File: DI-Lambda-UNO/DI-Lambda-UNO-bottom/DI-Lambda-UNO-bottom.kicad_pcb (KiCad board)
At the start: 2 copper layers, 38.2 x 128.2 mm, 53 parts, among them J1 CONN_02X04, J10 CONN_02X04, J11 CONN_02X04, J13 CONN_02X04, J15 CONN_01X06, J16 CONN_01X06, J17 CONN_02X03, J18 USB_OTG, J2 Conn_01X01, J3 CONN_02X04, J4 Conn_01X01, J5 CONN_02X04, J6 CONN_02X04, J7 CONN_02X04, J8 CONN_02X04, J9 CONN_02X04, Q1 AO3400, SW1 RESET, U2 USBLC6-2SC6, U3 ATMEGA32U4-MU, U4 3.3v LDO, U5 AP3032, Y1 8Mhz

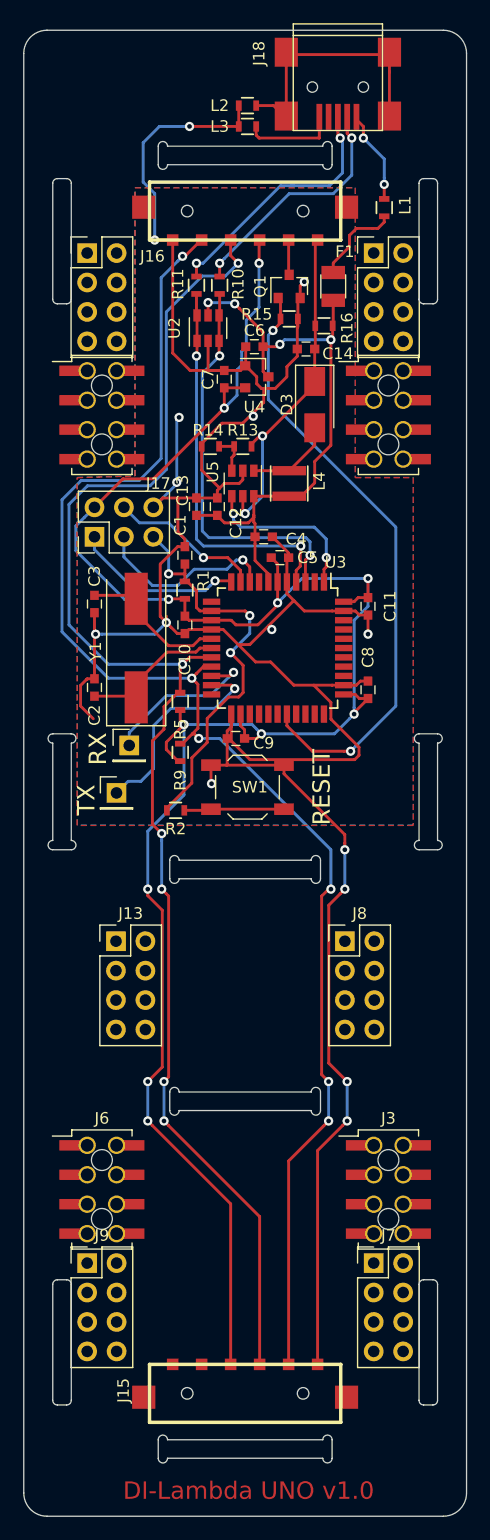
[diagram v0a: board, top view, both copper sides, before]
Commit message: Update connectors on the bottom plate
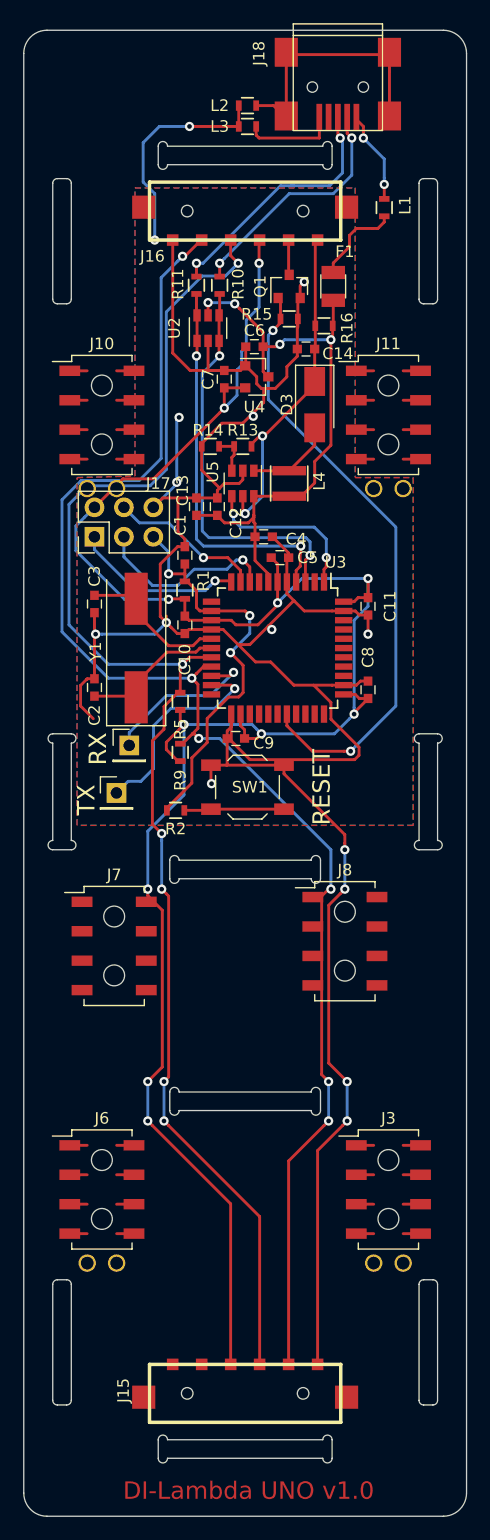
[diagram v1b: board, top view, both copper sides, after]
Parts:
- removed J1, J13, J5, J9: CONN_02X04, Pin_Headers:Pin_Header_Straight_2x04_Pitch2.54mm
- J10, J11, J3, J6: value CONN_02X04 -> CONN_02X05; footprint Female_socket_pitch254_smt_through-board:Pin_Header_Straight_2x04_Pitch2.54mm_SMD -> Female_socket_pitch254_smt_through-board:Pin_Header_Straight_2x04_Pitch2.54mm_SMD_2THT
- J7, J8: footprint Pin_Headers:Pin_Header_Straight_2x04_Pitch2.54mm -> Female_socket_pitch254_smt_through-board:Pin_Header_Straight_2x04_Pitch2.54mm_SMD
- moved J7 35.4 mm to (139.1, 115.0)

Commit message: Move spring connectors 0.3mm back on the bottom plate
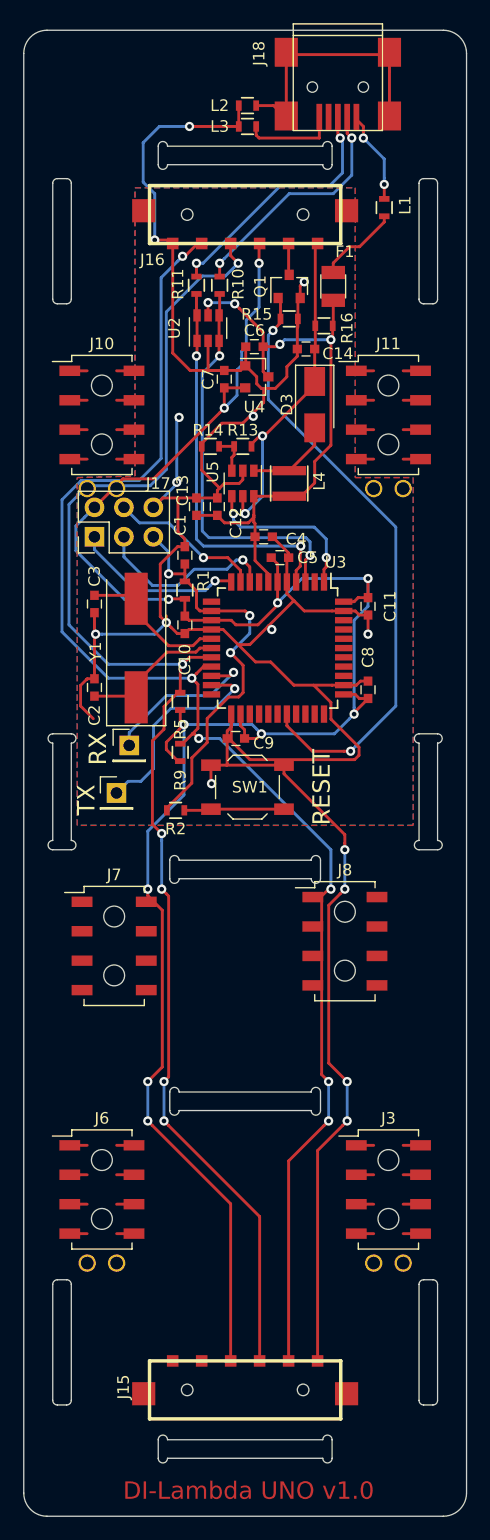
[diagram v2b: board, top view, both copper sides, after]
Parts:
- moved J16 0.30 mm to (150.4, 51.9)
- moved J15 0.30 mm to (150.4, 153.3)
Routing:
- net Net-(F1-Pad2): track 7.76 -> 7.18 mm
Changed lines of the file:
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@@
     (thickness 1.6)
     (drawings 106)
-    (tracks 628)
+    (tracks 625)
     (zones 0)
     (modules 49)
@@
   )
   (module Spring-contact-connector-2:Spring-contact-connector-2.5x6 (layer F.Cu)
-    (at 150.355 51.57 180)
+    (at 150.355 51.87 180)
     (fp_text reference J16 (at 8 -3.9) (layer F.SilkS)
       (effects (font (size 1 1) (thickness 0.15)))
@@
   )
   (module Spring-contact-connector-2:Spring-contact-connector-2.5x6 (layer F.Cu)
-    (at 150.355 153.57)
+    (at 150.355 153.27)
     (fp_text reference J15 (at -10.5 -0.25 90) (layer F.SilkS)
       (effects (font (size 1 1) (thickness 0.15)))
@@
   (segment (start 148.155 97.07) (end 157.755 106.67) (width 0.25) (layer B.Cu) (net 64))
   (segment (start 157.755 106.67) (end 157.755 110.07) (width 0.25) (layer B.Cu) (net 64))
+  (segment (start 157.955 56.87) (end 157.955 56.05) (width 0.25) (layer F.Cu) (net 68))
+  (segment (start 162.355 52.52) (end 162.355 52.02) (width 0.25) (layer F.Cu) (net 68))
+  (segment (start 157.955 56.05) (end 159.355 54.65) (width 0.25) (layer F.Cu) (net 68))
+  (segment (start 159.355 54.65) (end 160.225 54.65) (width 0.25) (layer F.Cu) (net 68))
+  (segment (start 160.225 54.65) (end 162.355 52.52) (width 0.25) (layer F.Cu) (net 68))
   (segment (start 142.355 104.47) (end 143.155 105.27) (width 0.25) (layer F.Cu) (net 72))
   (via (at 143.155 105.27) (size 0.8) (drill 0.4) (layers F.Cu B.Cu) (net 72))
@@
   (segment (start 149.055282 83.47) (end 149.155282 83.57) (width 0.25) (layer F.Cu) (net 67))
   (via (at 147.755 83.47) (size 0.8) (drill 0.4) (layers F.Cu B.Cu) (net 67))
-  (segment (start 159.955 53.07) (end 161.355 53.07) (width 0.25) (layer F.Cu) (net 68))
-  (segment (start 162.355 52.02) (end 162.355 52.52) (width 0.25) (layer F.Cu) (net 68))
-  (segment (start 162.355 52.52) (end 161.805 53.07) (width 0.25) (layer F.Cu) (net 68))
-  (segment (start 161.805 53.07) (end 161.355 53.07) (width 0.25) (layer F.Cu) (net 68))
-  (segment (start 159.355 53.67) (end 159.955 53.07) (width 0.25) (layer F.Cu) (net 68))
-  (segment (start 159.355 54.65) (end 159.355 53.67) (width 0.25) (layer F.Cu) (net 68))
-  (segment (start 157.955 56.87) (end 157.955 56.05) (width 0.25) (layer F.Cu) (net 68))
-  (segment (start 157.955 56.05) (end 159.355 54.65) (width 0.25) (layer F.Cu) (net 68))
   (segment (start 162.355 48.704315) (end 162.355 49.27) (width 0.25) (layer B.Cu) (net 69))
   (segment (start 162.355 47.073794) (end 162.355 48.704315) (width 0.25) (layer B.Cu) (net 69))

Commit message: Fix up the routing after connector update on the bottom plate
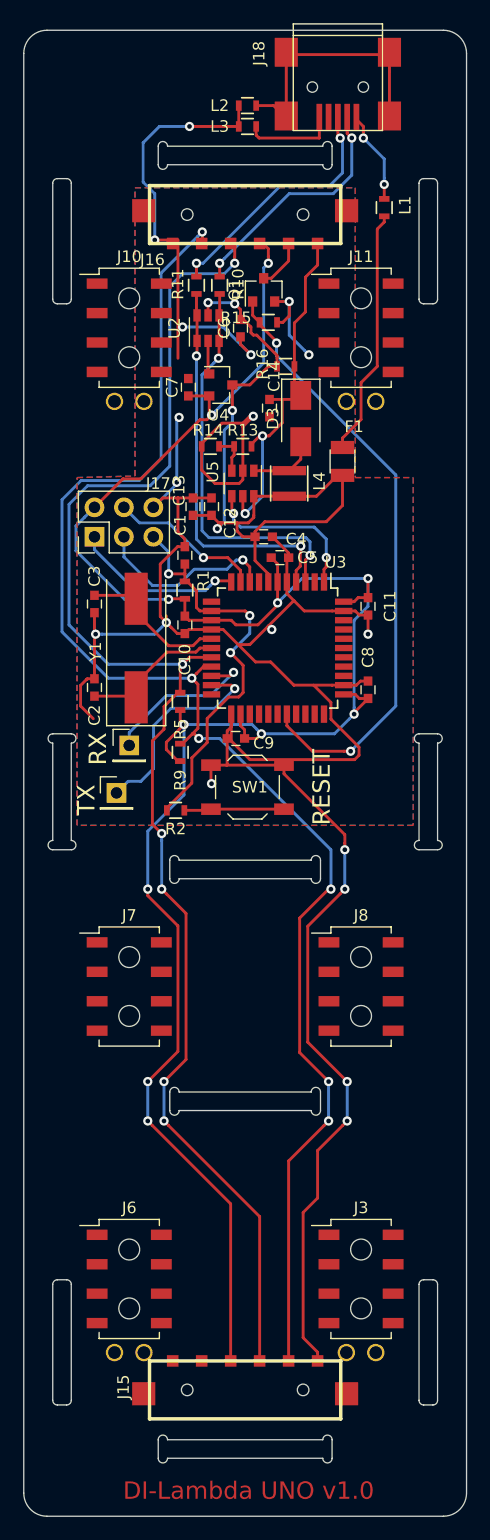
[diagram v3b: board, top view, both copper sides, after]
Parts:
- moved F1 15.1 mm to (158.8, 73.2)
- moved J3 8.07 mm to (160.4, 143.7)
- moved J6 8.07 mm to (140.4, 143.7)
- moved J11 7.88 mm to (160.4, 61.6)
- moved J10 7.88 mm to (140.4, 61.6)
- moved C14 5.99 mm to (152.5, 68.6), turned to 270 degrees
- moved R16 4.81 mm to (153.9, 65.0), turned to 0 degrees
- moved J8 4.15 mm to (160.4, 118.5)
- moved J7 3.73 mm to (140.4, 118.5)
- moved C7 3.18 mm to (145.5, 66.8)
- moved U4 3.18 mm to (148.3, 66.6)
- moved Q1 2.22 mm to (152.0, 58.4)
- moved C6 2.00 mm to (150.0, 61.7), turned to 90 degrees
- moved R15 1.82 mm to (152.4, 61.2)
- moved D3 1.70 mm to (155.2, 69.5)
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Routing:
- net Net-(F1-Pad2): track 7.18 -> 21.4 mm
- net /VBUS: track 52.7 -> 64.1 mm
- net /SDA: track 126.1 -> 128.9 mm
- net /VLED: track 29.7 -> 32.3 mm
- net GND: track 251.8 -> 249.3 mm, vias 15 -> 18
- net /SCL: track 123.8 -> 125.8 mm
- net /SW: track 7.66 -> 5.96 mm
- net Net-(J6-Pad8): track 1.50 -> 0.00 mm
- net Net-(J6-Pad7): track 1.50 -> 0.00 mm
- net Net-(J6-Pad6): track 1.50 -> 0.00 mm
- net Net-(J6-Pad5): track 1.50 -> 0.00 mm
- net Net-(J6-Pad4): track 1.50 -> 0.00 mm
- net Net-(J6-Pad3): track 1.50 -> 0.00 mm
- net Net-(J6-Pad2): track 1.50 -> 0.00 mm
- net Net-(J6-Pad1): track 1.50 -> 0.00 mm
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
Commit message: Update main plate dimensions
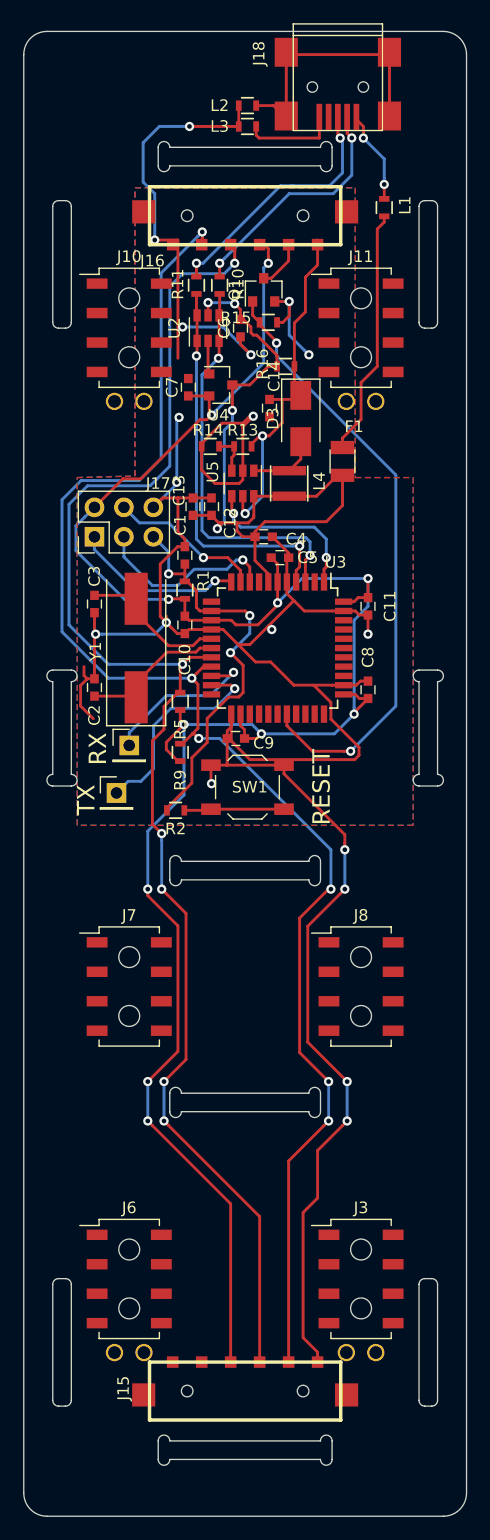
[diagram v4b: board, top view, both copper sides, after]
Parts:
- moved J16 0.10 mm to (150.4, 52.0)
- moved J15 0.10 mm to (150.4, 153.4)
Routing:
- net GND: track 249.3 -> 250.4 mm
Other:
- board size 38.2 x 128.2 mm -> 38.2 x 128.1 mm
- board text added: "DI-Lambda UNO v1.1"
- board text removed: "DI-Lambda UNO v1.0"

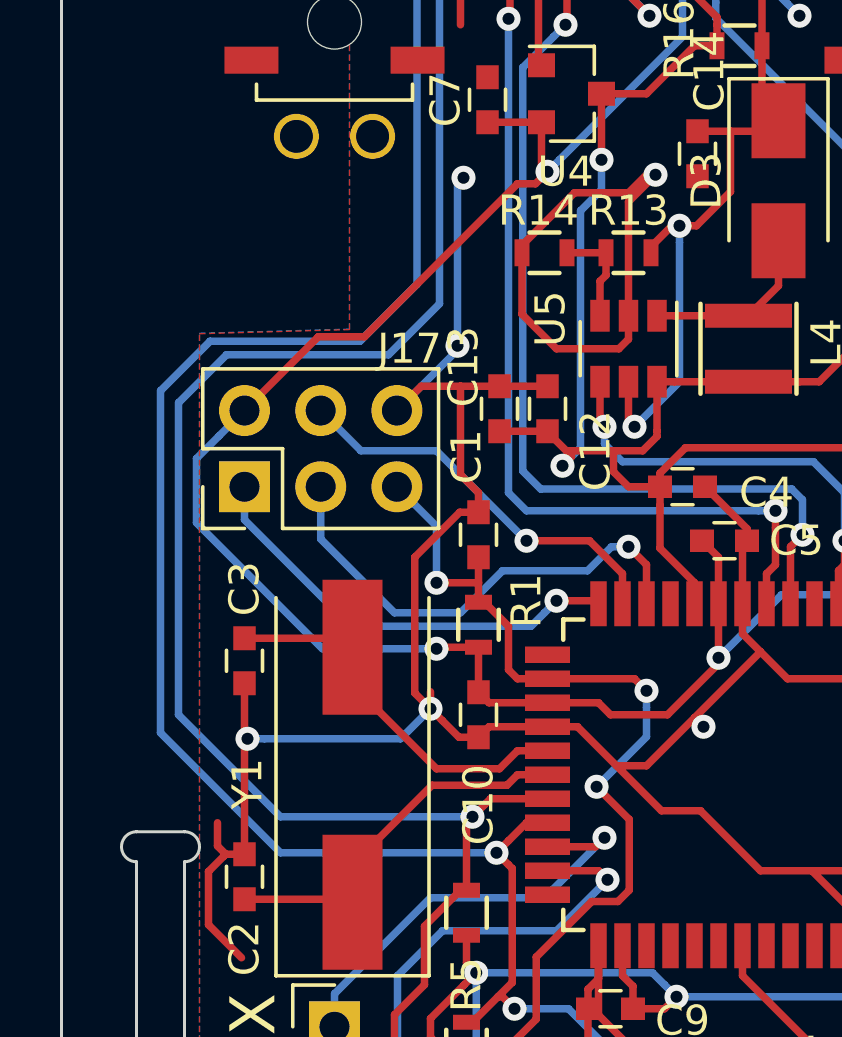
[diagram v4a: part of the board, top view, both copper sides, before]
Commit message: Use SMT pin header for ISP on the bottom plate
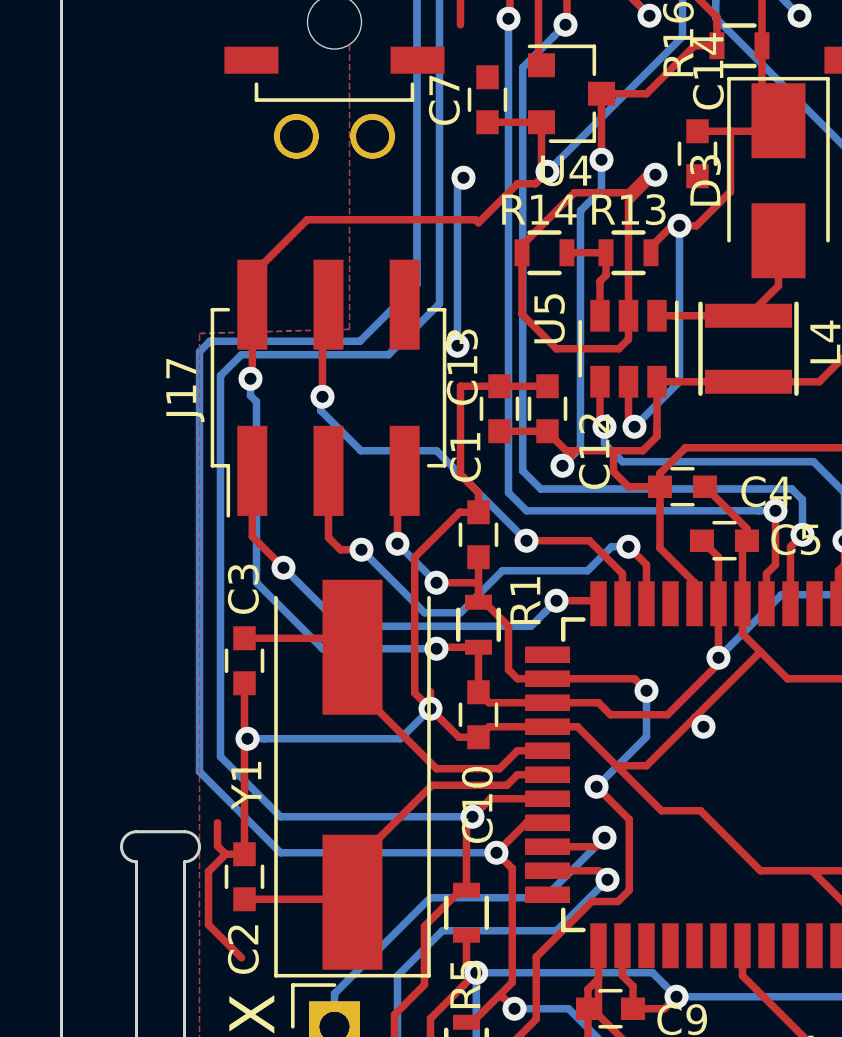
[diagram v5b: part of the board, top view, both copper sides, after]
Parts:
- J17: footprint Pin_Headers:Pin_Header_Straight_2x03_Pitch2.54mm -> Pin_Headers:Pin_Header_Straight_2x03_Pitch2.54mm_SMD
- moved J17 4.33 mm to (140.2, 76.4)
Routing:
- net GND: track 250.4 -> 245.1 mm
- net /MOSI: track 13.3 -> 17.0 mm, vias 1 -> 2
- net /SCL: track 125.8 -> 124.3 mm
- net /VCC: track 180.6 -> 181.7 mm, vias 11 -> 12
- net /SDA: track 128.9 -> 127.9 mm
- net /SCK: track 16.1 -> 15.4 mm, vias 1 -> 2
- net /RST: track 35.5 -> 36.1 mm, vias 3 -> 4
- net /MISO: track 14.8 -> 14.5 mm, vias 1 -> 2
